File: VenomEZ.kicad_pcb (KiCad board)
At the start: 2 copper layers, 72 x 42 mm, 42 parts, among them CN1 HC-XH-5A-G, CN10 HC-XH-2A-G, CN2 HC-PH-8A-G, CN3 HC-XH-8A-G, CN4 HC-XH-8A-G, CN5 HC-XH-2A-G, CN6 HC-PH-7A-G, CN7 HC-XH-2A-G, CN8 HC-XH-2A-G, CN9 HC-XH-2A-G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

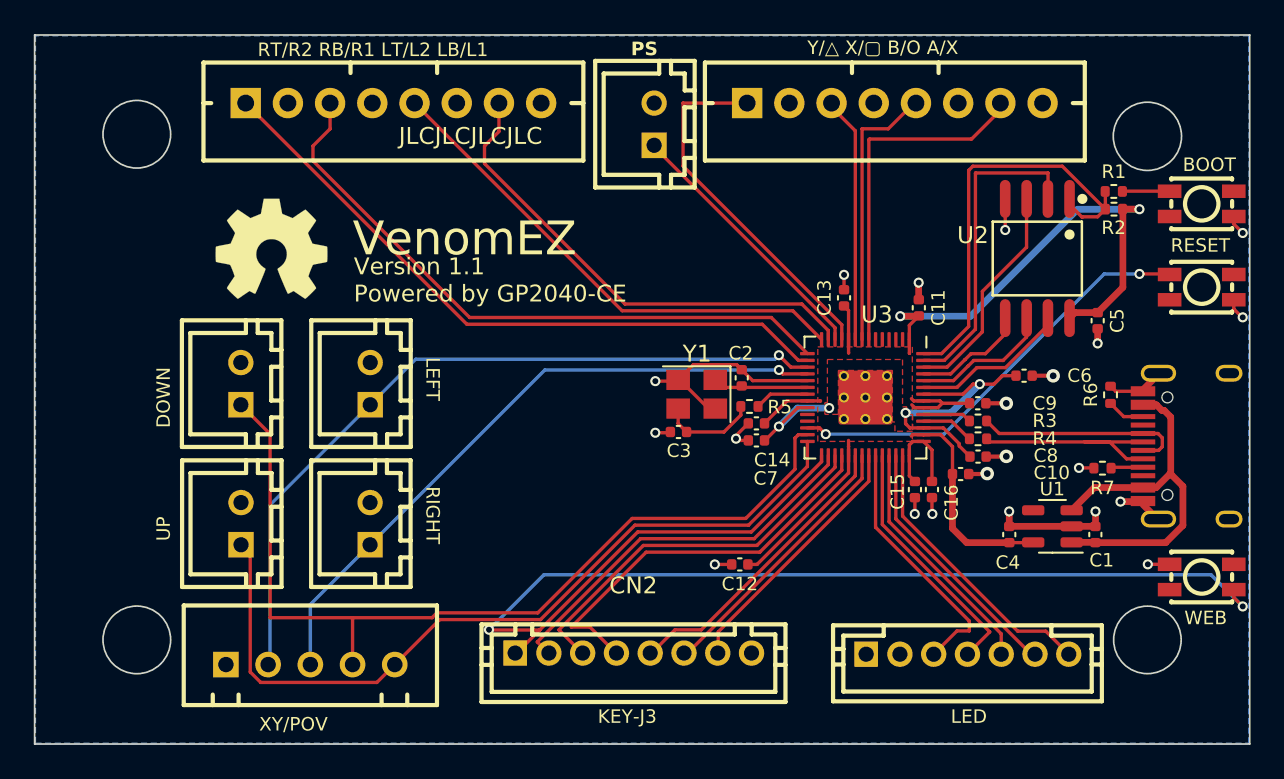
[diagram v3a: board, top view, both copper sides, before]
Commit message: Most likely fixed LED. Mounting holes enlarged.
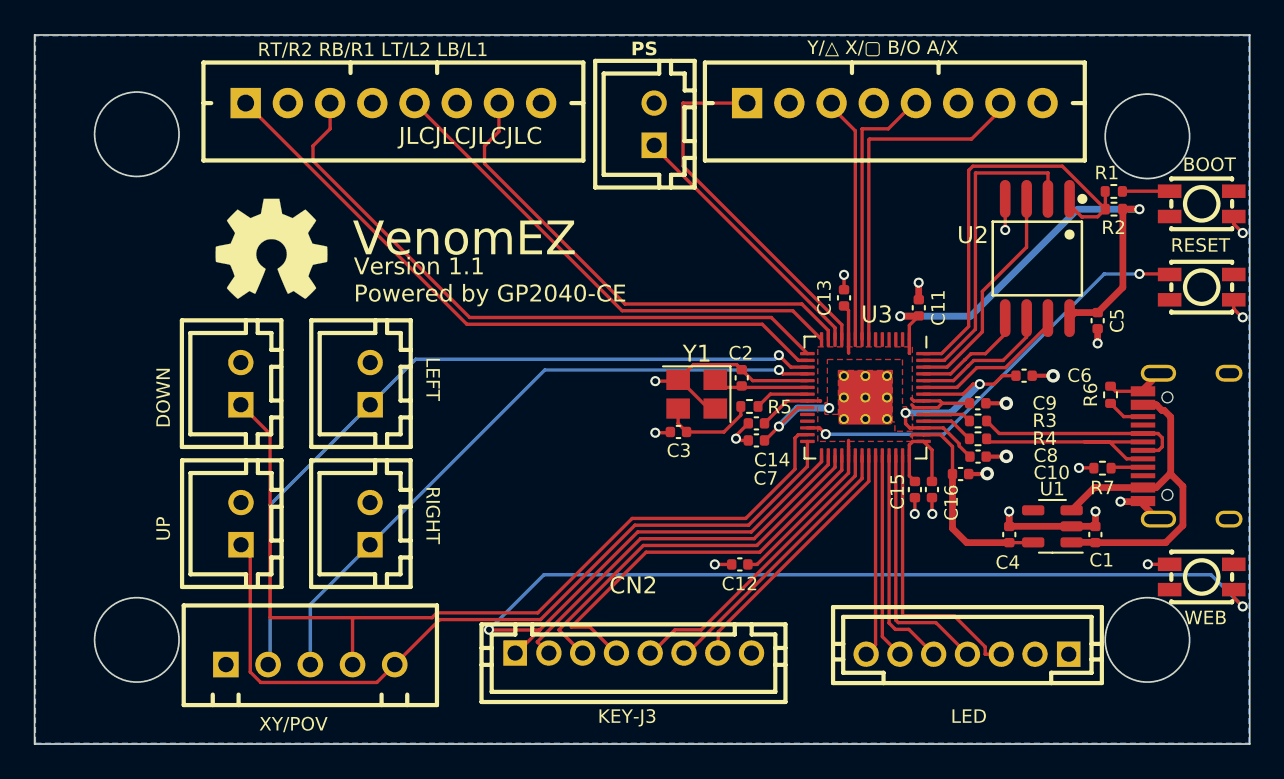
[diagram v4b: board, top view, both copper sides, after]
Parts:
- turned CN6 to 180 degrees
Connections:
- U3 pad 37: TURBO LED -> PLED 1
- U3 pad 38: PLED 4 -> PLED 2
- U3 pad 40: PLED 2 -> PLED 4
- U3 pad 41: PLED 1 -> TURBO LED
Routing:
- net PLED 1: track 16.8 -> 12.0 mm
- net PLED 2: track 15.3 -> 12.2 mm
- net PLED 3: track 14.5 -> 13.3 mm
- net TURBO LED: track 15.4 -> 16.5 mm
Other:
- outline, holes or cut-outs redrawn
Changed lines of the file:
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@@
     (property "ki_keywords" "R resistor")
     (attr smd)
-    (fp_text reference "R1" (at 0 -1.17) (layer "F.SilkS")
+    (fp_text reference "R1" (at -0.411254 -1.092424) (layer "F.SilkS")
         (effects (font (size 0.8 0.8) (thickness 0.15)))
     )
@@
   )
   (footprint "easyeda2kicad:CONN-TH_7P-P2.00_PH-7A" (layer "F.Cu")
-    (at 132.7437 111.3819)
+    (at 132.7437 111.3819 180)
     (property "JLC Part" "Extended Part")
     (property "LCSC Part" "C10398")
@@
     (fp_circle (center 6 0) (end 6.18 0)
       (stroke (width 0.35) (type solid)) (fill none) (layer "F.Fab"))
-    (pad "1" thru_hole rect (at -6 0 180) (size 1.4 1.5) (drill 0.900024) (layers "*.Cu" "*.Paste" "*.Mask")
+    (pad "1" thru_hole rect (at -6 0) (size 1.4 1.5) (drill 0.900024) (layers "*.Cu" "*.Paste" "*.Mask")
       (net 2 "GND") (pinfunction "1") (pintype "unspecified"))
-    (pad "2" thru_hole circle (at -4 0 180) (size 1.5 1.5) (drill 0.900024) (layers "*.Cu" "*.Paste" "*.Mask")
+    (pad "2" thru_hole circle (at -4 0) (size 1.5 1.5) (drill 0.900024) (layers "*.Cu" "*.Paste" "*.Mask")
       (net 27 "unconnected-(CN6-Pad2)") (pinfunction "2") (pintype "unspecified+no_connect"))
-    (pad "3" thru_hole circle (at -2 0 180) (size 1.5 1.5) (drill 0.900024) (layers "*.Cu" "*.Paste" "*.Mask")
+    (pad "3" thru_hole circle (at -2 0) (size 1.5 1.5) (drill 0.900024) (layers "*.Cu" "*.Paste" "*.Mask")
       (net 10 "TURBO LED") (pinfunction "3") (pintype "unspecified"))
-    (pad "4" thru_hole circle (at 0 0 180) (size 1.5 1.5) (drill 0.900024) (layers "*.Cu" "*.Paste" "*.Mask")
+    (pad "4" thru_hole circle (at 0 0) (size 1.5 1.5) (drill 0.900024) (layers "*.Cu" "*.Paste" "*.Mask")
       (net 11 "PLED 4") (pinfunction "4") (pintype "unspecified"))
-    (pad "5" thru_hole circle (at 2 0 180) (size 1.5 1.5) (drill 0.900024) (layers "*.Cu" "*.Paste" "*.Mask")
+    (pad "5" thru_hole circle (at 2 0) (size 1.5 1.5) (drill 0.900024) (layers "*.Cu" "*.Paste" "*.Mask")
       (net 12 "PLED 3") (pinfunction "5") (pintype "unspecified"))
-    (pad "6" thru_hole circle (at 4 0 180) (size 1.5 1.5) (drill 0.900024) (layers "*.Cu" "*.Paste" "*.Mask")
+    (pad "6" thru_hole circle (at 4 0) (size 1.5 1.5) (drill 0.900024) (layers "*.Cu" "*.Paste" "*.Mask")
       (net 13 "PLED 2") (pinfunction "6") (pintype "unspecified"))
-    (pad "7" thru_hole circle (at 6 0 180) (size 1.5 1.5) (drill 0.900024) (layers "*.Cu" "*.Paste" "*.Mask")
+    (pad "7" thru_hole circle (at 6 0) (size 1.5 1.5) (drill 0.900024) (layers "*.Cu" "*.Paste" "*.Mask")
       (net 14 "PLED 1") (pinfunction "7") (pintype "unspecified"))
     (model "${KIPRJMOD}/easyeda2kicad.3dshapes/CONN-TH_7P-P2.00_PH-7A.wrl"
@@
       (net 9 "PS4 MODE") (pinfunction "GPIO24") (pintype "bidirectional"))
     (pad "37" smd roundrect (at 3.4375 -0.6 270) (size 0.875 0.2) (layers "F.Cu" "F.Paste" "F.Mask") (roundrect_rratio 0.25)
-      (net 10 "TURBO LED") (pinfunction "GPIO25") (pintype "bidirectional"))
+      (net 14 "PLED 1") (pinfunction "GPIO25") (pintype "bidirectional"))
     (pad "38" smd roundrect (at 3.4375 -1 270) (size 0.875 0.2) (layers "F.Cu" "F.Paste" "F.Mask") (roundrect_rratio 0.25)
-      (net 11 "PLED 4") (pinfunction "GPIO26_ADC0") (pintype "bidirectional"))
+      (net 13 "PLED 2") (pinfunction "GPIO26_ADC0") (pintype "bidirectional"))
     (pad "39" smd roundrect (at 3.4375 -1.4 270) (size 0.875 0.2) (layers "F.Cu" "F.Paste" "F.Mask") (roundrect_rratio 0.25)
       (net 12 "PLED 3") (pinfunction "GPIO27_ADC1") (pintype "bidirectional"))
     (pad "40" smd roundrect (at 3.4375 -1.8 270) (size 0.875 0.2) (layers "F.Cu" "F.Paste" "F.Mask") (roundrect_rratio 0.25)
-      (net 13 "PLED 2") (pinfunction "GPIO28_ADC2") (pintype "bidirectional"))
+      (net 11 "PLED 4") (pinfunction "GPIO28_ADC2") (pintype "bidirectional"))
     (pad "41" smd roundrect (at 3.4375 -2.2 270) (size 0.875 0.2) (layers "F.Cu" "F.Paste" "F.Mask") (roundrect_rratio 0.25)
-      (net 14 "PLED 1") (pinfunction "GPIO29_ADC3") (pintype "bidirectional"))
+      (net 10 "TURBO LED") (pinfunction "GPIO29_ADC3") (pintype "bidirectional"))
     (pad "42" smd roundrect (at 3.4375 -2.6 270) (size 0.875 0.2) (layers "F.Cu" "F.Paste" "F.Mask") (roundrect_rratio 0.25)
       (net 34 "+3V3") (pinfunction "IOVDD") (pintype "power_in"))
@@
     )
   )
-  (gr_circle (center 83.547094 80.586385) (end 85.484596 81.093787)
+  (gr_circle (center 83.547094 80.586385) (end 86.047094 80.586385)
     (stroke (width 0.1) (type default)) (fill none) (layer "Edge.Cuts"))
-  (gr_circle (center 83.547094 110.534209) (end 85.484594 110.027136)
+  (gr_circle (center 83.547094 110.534209) (end 86.047094 110.534209)
     (stroke (width 0.1) (type default)) (fill none) (layer "Edge.Cuts"))
-  (gr_circle (center 143.401941 80.708788) (end 144.442693 78.976203)
+  (gr_circle (center 143.401941 80.708788) (end 145.901941 80.708788)
     (stroke (width 0.1) (type default)) (fill none) (layer "Edge.Cuts"))
-  (gr_circle (center 143.401941 110.534209) (end 144.23213 112.353265)
+  (gr_circle (center 143.401941 110.534209) (end 145.901941 110.534209)
     (stroke (width 0.1) (type default)) (fill none) (layer "Edge.Cuts"))
   (gr_rect (start 77.492988 74.707243) (end 149.459652 116.701911)
@@
   (segment (start 126.90151 101.144086) (end 126.90151 99.6175) (width 0.2) (layer "F.Cu") (net 9))
   (segment (start 117.983 111.373) (end 117.983 110.062597) (width 0.2) (layer "F.Cu") (net 9))
-  (segment (start 130.7437 111.3819) (end 132.124127 110.001473) (width 0.2) (layer "F.Cu") (net 10))
-  (segment (start 132.124127 110.001473) (end 132.852228 110.001473) (width 0.2) (layer "F.Cu") (net 10))
-  (segment (start 132.852228 109.41467) (end 127.30151 103.863952) (width 0.2) (layer "F.Cu") (net 10))
-  (segment (start 127.30151 103.863952) (end 127.30151 99.6175) (width 0.2) (layer "F.Cu") (net 10))
-  (segment (start 132.852228 110.001473) (end 132.852228 109.41467) (width 0.2) (layer "F.Cu") (net 10))
-  (segment (start 127.70151 103.698269) (end 127.70151 99.6175) (width 0.2) (layer "F.Cu") (net 11))
-  (segment (start 132.7437 111.3819) (end 134.06442 110.061179) (width 0.2) (layer "F.Cu") (net 11))
-  (segment (start 134.06442 110.061179) (end 127.70151 103.698269) (width 0.2) (layer "F.Cu") (net 11))
-  (segment (start 134.7437 111.3819) (end 134.7437 110.174773) (width 0.2) (layer "F.Cu") (net 12))
-  (segment (start 128.10151 103.532583) (end 128.10151 99.6175) (width 0.2) (layer "F.Cu") (net 12))
-  (segment (start 134.7437 110.174773) (end 128.10151 103.532583) (width 0.2) (layer "F.Cu") (net 12))
-  (segment (start 128.50151 103.366897) (end 128.50151 99.6175) (width 0.2) (layer "F.Cu") (net 13))
-  (segment (start 136.7437 111.3819) (end 136.516513 111.3819) (width 0.2) (layer "F.Cu") (net 13))
-  (segment (start 136.516513 111.3819) (end 128.50151 103.366897) (width 0.2) (layer "F.Cu") (net 13))
-  (segment (start 138.7437 111.3819) (end 137.379707 110.017907) (width 0.2) (layer "F.Cu") (net 14))
-  (segment (start 137.379707 110.017907) (end 135.718206 110.017907) (width 0.2) (layer "F.Cu") (net 14))
-  (segment (start 128.90151 103.201211) (end 128.90151 99.6175) (width 0.2) (layer "F.Cu") (net 14))
-  (segment (start 135.718206 110.017907) (end 128.90151 103.201211) (width 0.2) (layer "F.Cu") (net 14))
+  (segment (start 131.958941 109.112216) (end 128.90151 109.112216) (width 0.2) (layer "F.Cu") (net 10))
+  (segment (start 134.7437 111.3819) (end 133.7937 111.3819) (width 0.2) (layer "F.Cu") (net 10))
+  (segment (start 128.90151 109.112216) (end 128.90151 99.6175) (width 0.2) (layer "F.Cu") (net 10))
+  (segment (start 133.7937 111.3819) (end 133.7937 110.946975) (width 0.2) (layer "F.Cu") (net 10))
+  (segment (start 133.7937 110.946975) (end 131.958941 109.112216) (width 0.2) (layer "F.Cu") (net 10))
+  (segment (start 132.7437 111.3819) (end 130.874016 109.512216) (width 0.2) (layer "F.Cu") (net 11))
+  (segment (start 128.643574 109.512216) (end 128.50151 109.370152) (width 0.2) (layer "F.Cu") (net 11))
+  (segment (start 130.874016 109.512216) (end 128.643574 109.512216) (width 0.2) (layer "F.Cu") (net 11))
+  (segment (start 128.50151 109.370152) (end 128.50151 99.6175) (width 0.2) (layer "F.Cu") (net 11))
+  (segment (start 129.274016 109.912216) (end 128.477888 109.912216) (width 0.2) (layer "F.Cu") (net 12))
+  (segment (start 130.7437 111.3819) (end 129.274016 109.912216) (width 0.2) (layer "F.Cu") (net 12))
+  (segment (start 128.477888 109.912216) (end 128.10151 109.535838) (width 0.2) (layer "F.Cu") (net 12))
+  (segment (start 128.10151 109.535838) (end 128.10151 99.6175) (width 0.2) (layer "F.Cu") (net 12))
+  (segment (start 128.7437 111.3819) (end 127.70151 110.33971) (width 0.2) (layer "F.Cu") (net 13))
+  (segment (start 127.70151 110.33971) (end 127.70151 99.6175) (width 0.2) (layer "F.Cu") (net 13))
+  (segment (start 127.30151 110.82409) (end 127.30151 99.6175) (width 0.2) (layer "F.Cu") (net 14))
+  (segment (start 126.7437 111.3819) (end 127.30151 110.82409) (width 0.2) (layer "F.Cu") (net 14))
   (segment (start 121.577177 93.673464) (end 122.283713 94.38) (width 0.2) (layer "F.Cu") (net 15))
   (segment (start 122.283713 94.38) (end 123.26401 94.38) (width 0.2) (layer "F.Cu") (net 15))

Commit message: Move web button up to the boot and reset buttons
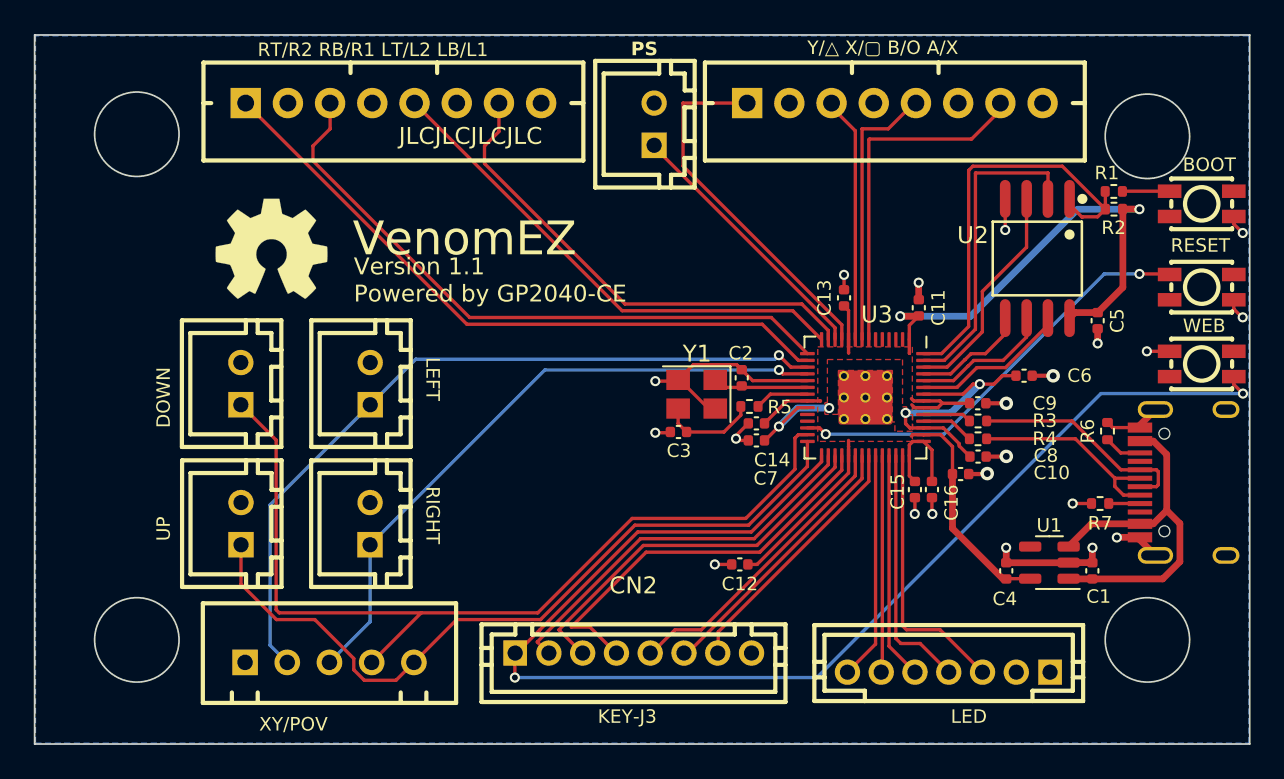
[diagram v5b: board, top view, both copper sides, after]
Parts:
- moved SW1 12.6 mm to (146.6, 94.2)
- moved C1 2.16 mm to (140.1, 106.4)
- moved C4 2.16 mm to (135.0, 106.4)
- moved R6 2.16 mm to (141.0, 98.2)
- moved U1 2.16 mm to (137.6, 106.0)
- moved USB1 2.16 mm to (150.7, 101.2)
- moved R7 2.10 mm to (140.6, 102.5)
- moved CN6 1.54 mm to (131.6, 112.4)
- moved CN1 1.14 mm to (95.0, 111.9)
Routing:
- net UP: track 47.8 -> 45.4 mm
- net S2 (START): track 74.2 -> 76.0 mm
- net PLED 1: track 12.0 -> 13.5 mm
- net GND: track 45.0 -> 46.0 mm
- net D-: track 13.2 -> 12.2 mm
- net D+: track 12.6 -> 13.3 mm
- net +3V3: track 70.9 -> 71.6 mm
- net PLED 2: track 12.2 -> 12.9 mm
- net DOWN: track 53.5 -> 54.2 mm
- net RIGHT: track 38.8 -> 38.3 mm
- net TURBO LED: track 16.5 -> 16.0 mm

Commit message: Add gp2040-ce logo to rear of board
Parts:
- added G***: LOGO, GP2040-CE:gp2040-ce-logo, B.Cu at (99.1, 86.4)
